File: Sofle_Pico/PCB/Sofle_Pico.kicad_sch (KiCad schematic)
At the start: 81 parts, among them J1 Pimaroni Trackball, J2 4PIN, J3 OLED, J5 Conn_01x05_Socket, J6 Conn_01x05_Socket, Q1 TIP120, SW1 SW_PUSH_LED, SW10 SW_PUSH_LED, SW11 SW_PUSH_LED, SW12 SW_PUSH_LED, SW13 SW_PUSH_LED, SW14 SW_PUSH_LED, SW15 SW_PUSH_LED, SW16 SW_PUSH_LED, SW17 SW_PUSH_LED, SW18 SW_PUSH_LED, SW19 SW_PUSH_LED, SW2 SW_PUSH_LED, SW20 SW_PUSH_LED, SW21 SW_PUSH_LED, SW22 SW_PUSH_LED, SW23 SW_PUSH_LED, SW24 SW_PUSH_LED, SW25 Rotary_Encoder_Switch, SW26 SW_PUSH_LED, SW27 SW_PUSH_LED, SW28 SW_PUSH_LED, SW29 SW_PUSH_LED, SW3 SW_PUSH_LED, SW30 SW_PUSH_LED, SW4 SW_PUSH_LED, SW5 SW_PUSH_LED, SW6 SW_PUSH_LED, SW7 SW_PUSH_LED, SW8 SW_PUSH_LED, SW9 SW_PUSH_LED, U1 SN74AHCT1G125, U3 Pico

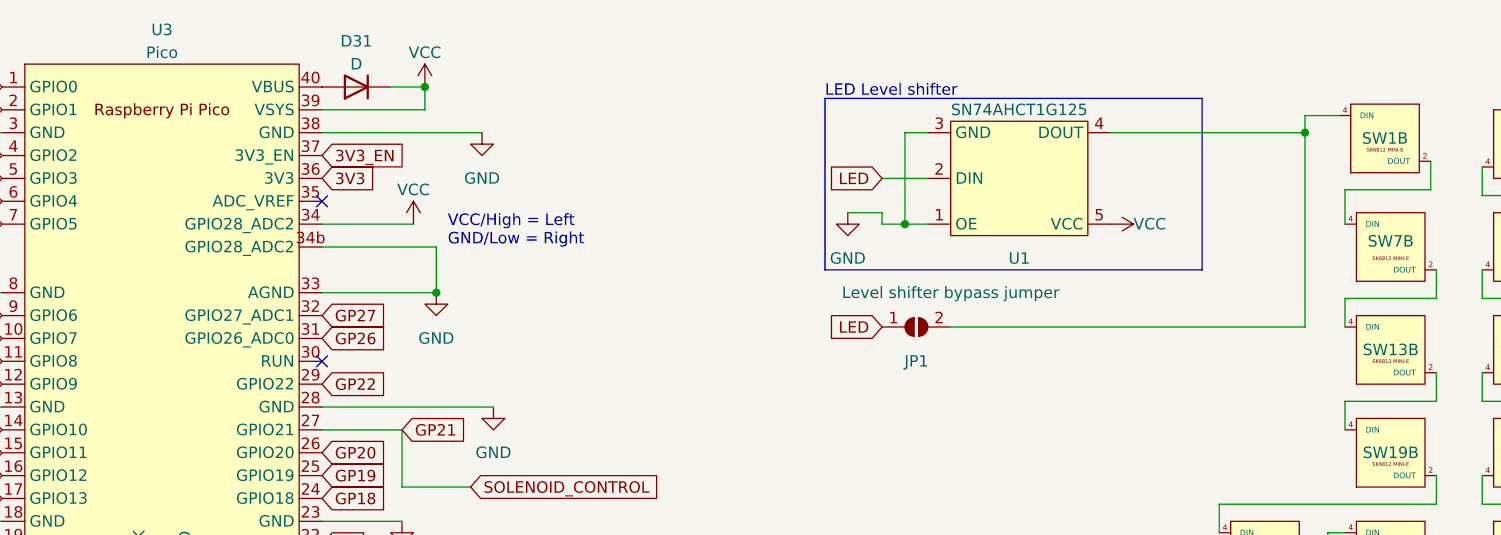
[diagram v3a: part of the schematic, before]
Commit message: Revised LED footprint for better teardrops Tweaked patch bay footprints Tweaked traces for improved zone connections
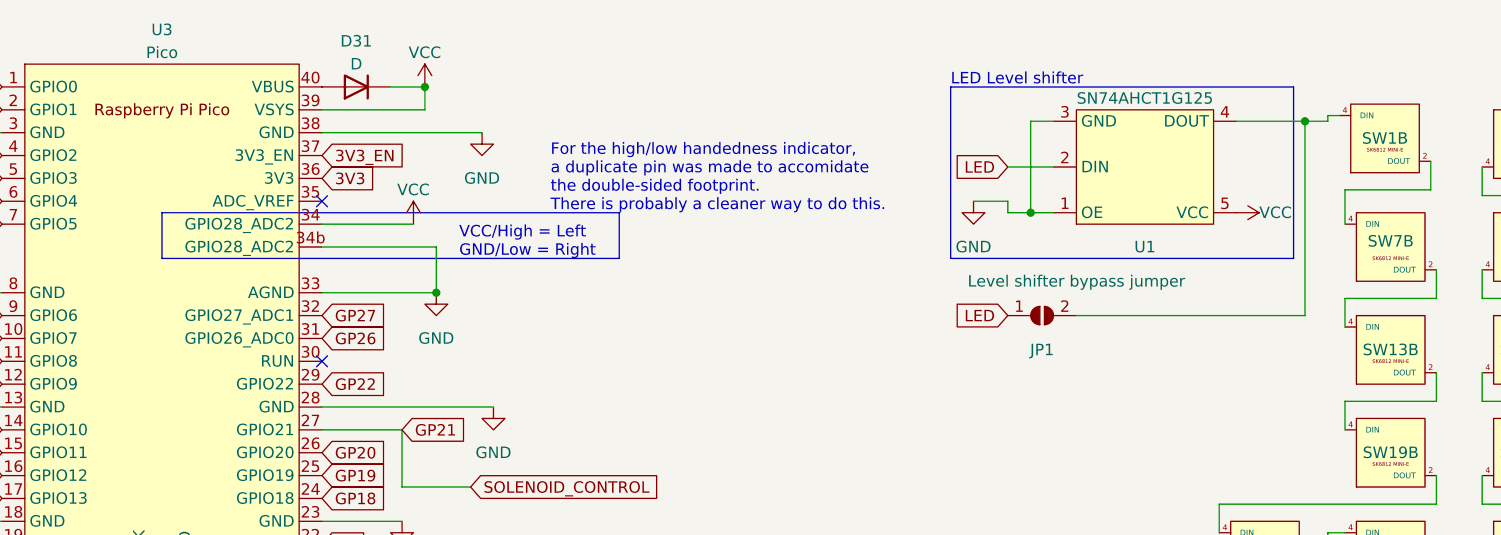
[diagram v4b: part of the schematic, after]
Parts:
- J5: footprint Connector_PinHeader_2.54mm:PinHeader_1x05_P2.54mm_Vertical -> Sofle_Pico:PinHeader_1x05_P2.54mm_Vertical_one-dead
- J6: footprint Connector_PinHeader_2.54mm:PinHeader_1x05_P2.54mm_Vertical -> Sofle_Pico:PinHeader_1x05_P2.54mm_Vertical
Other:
- note added: "For the high/low handedness indicator, a duplicate pin was made to accomidate the double-sided footprint. There is probably a cleaner way to do this."
- moved on the sheet: JP1, U1
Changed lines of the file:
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@@
   (title_block
     (title "Sofle Pico")
-    (date "2023-09-08")
-    (rev "v3.5.1")
+    (date "2023-12-15")
+    (rev "v3.5.2")
     (comment 1 "https://github.com/josefadamcik/SofleKeyboard")
     (comment 2 "Based on the Sofle by Josef Adamcik")
@@
   (junction (at 240.03 114.3) (diameter 0) (color 0 0 0 0)
   )
-  (junction (at 127 36.83) (diameter 0) (color 0 0 0 0)
+  (junction (at 140.97 35.56) (diameter 0) (color 0 0 0 0)
   )
   (junction (at 143.51 139.7) (diameter 0) (color 0 0 0 0)
@@
   (junction (at 199.39 114.3) (diameter 0) (color 0 0 0 0)
   )
+  (junction (at 171.45 25.4) (diameter 0) (color 0 0 0 0)
+  )
   (junction (at 184.15 123.19) (diameter 0) (color 0 0 0 0)
   )
@@
   (junction (at 158.75 147.32) (diameter 0) (color 0 0 0 0)
   )
-  (junction (at 171.45 26.67) (diameter 0) (color 0 0 0 0)
-  )
   (junction (at 163.83 106.68) (diameter 0) (color 0 0 0 0)
   )
@@
     (stroke (width 0) (type default))
   )
+  (wire (pts (xy 171.45 25.4) (xy 173.99 25.4))
+    (stroke (width 0) (type default))
+  )
   (wire (pts (xy 184.15 139.7) (xy 184.15 156.21))
     (stroke (width 0) (type default))
@@
     (stroke (width 0) (type default))
   )
-  (wire (pts (xy 124.46 36.83) (xy 127 36.83))
+  (wire (pts (xy 138.43 35.56) (xy 140.97 35.56))
     (stroke (width 0) (type default))
   )
@@
     (stroke (width 0) (type default))
   )
-  (wire (pts (xy 149.86 26.67) (xy 171.45 26.67))
+  (wire (pts (xy 163.83 25.4) (xy 171.45 25.4))
     (stroke (width 0) (type default))
   )
@@
     (stroke (width 0) (type default))
   )
-  (wire (pts (xy 127 26.67) (xy 129.54 26.67))
+  (wire (pts (xy 140.97 25.4) (xy 143.51 25.4))
     (stroke (width 0) (type default))
   )
@@
     (stroke (width 0) (type default))
   )
-  (wire (pts (xy 171.45 24.765) (xy 175.26 24.765))
+  (wire (pts (xy 173.99 24.765) (xy 175.26 24.765))
     (stroke (width 0) (type default))
   )
@@
     (stroke (width 0) (type default))
   )
-  (wire (pts (xy 129.54 31.75) (xy 124.46 31.75))
+  (wire (pts (xy 143.51 30.48) (xy 138.43 30.48))
     (stroke (width 0) (type default))
   )
@@
     (stroke (width 0) (type default))
   )
-  (wire (pts (xy 171.45 26.67) (xy 171.45 24.765))
+  (wire (pts (xy 173.99 25.4) (xy 173.99 24.765))
     (stroke (width 0) (type default))
   )
@@
     (stroke (width 0) (type default))
   )
-  (wire (pts (xy 132.08 48.26) (xy 171.45 48.26))
+  (wire (pts (xy 146.05 46.99) (xy 171.45 46.99))
     (stroke (width 0) (type default))
   )
@@
     (stroke (width 0) (type default))
   )
-  (wire (pts (xy 120.65 35.56) (xy 124.46 35.56))
+  (wire (pts (xy 134.62 34.29) (xy 138.43 34.29))
     (stroke (width 0) (type default))
   )
@@
     (stroke (width 0) (type default))
   )
-  (wire (pts (xy 124.46 35.56) (xy 124.46 36.83))
+  (wire (pts (xy 138.43 34.29) (xy 138.43 35.56))
     (stroke (width 0) (type default))
   )
@@
     (stroke (width 0) (type default))
   )
-  (wire (pts (xy 171.45 26.67) (xy 171.45 48.26))
+  (wire (pts (xy 171.45 25.4) (xy 171.45 46.99))
     (stroke (width 0) (type default))
   )
@@
     (stroke (width 0) (type default))
   )
-  (wire (pts (xy 127 36.83) (xy 127 26.67))
+  (wire (pts (xy 140.97 35.56) (xy 140.97 25.4))
     (stroke (width 0) (type default))
   )
@@
     (stroke (width 0) (type default))
   )
-  (wire (pts (xy 127 36.83) (xy 129.54 36.83))
+  (wire (pts (xy 140.97 35.56) (xy 143.51 35.56))
     (stroke (width 0) (type default))
   )
@@
     (fill (type none))
   )
-  (rectangle (start 118.11 22.86) (end 160.02 41.91)
+  (rectangle (start 132.08 21.59) (end 170.18 40.64)
     (stroke (width 0) (type default))
     (fill (type none))
@@
     (fill (type none))
   )
+  (rectangle (start 44.45 35.56) (end 95.25 40.64)
+    (stroke (width 0) (type default))
+    (fill (type none))
+  )
   (rectangle (start 13.97 132.08) (end 54.61 156.21)
     (stroke (width 0) (type default))
@@
     (effects (font (size 1.27 1.27)) (justify left bottom))
   )
-  (text "LED Level shifter" (at 118.11 22.86 0)
+  (text "For the high/low handedness indicator, \na duplicate pin was made to accomidate \nthe double-sided footprint. \nThere is probably a cleaner way to do this."
+    (at 87.63 35.56 0)
+    (effects (font (size 1.27 1.27)) (justify left bottom))
+  )
+  (text "LED Level shifter" (at 132.08 21.59 0)
     (effects (font (size 1.27 1.27)) (justify left bottom))
   )
@@
     (effects (font (size 1.27 1.27)) (justify left bottom))
   )
-  (text "VCC/High = Left\nGND/Low = Right" (at 76.2 39.37 0)
+  (text "VCC/High = Left\nGND/Low = Right" (at 77.47 40.64 0)
     (effects (font (size 1.27 1.27)) (justify left bottom))
   )
@@
     )
   )
-  (global_label "LED" (shape input) (at 124.46 31.75 180) (fields_autoplaced)
+  (global_label "LED" (shape input) (at 138.43 30.48 180) (fields_autoplaced)
     (effects (font (size 1.27 1.27)) (justify right))
-    (property "Intersheetrefs" "${INTERSHEET_REFS}" (at 118.1071 31.75 0)
+    (property "Intersheetrefs" "${INTERSHEET_REFS}" (at 132.0771 30.48 0)
       (effects (font (size 1.27 1.27)) (justify right) hide)
     )
@@
     )
   )
-  (global_label "LED" (shape input) (at 124.46 48.26 180) (fields_autoplaced)
+  (global_label "LED" (shape input) (at 138.43 46.99 180) (fields_autoplaced)
     (effects (font (size 1.27 1.27)) (justify right))
-    (property "Intersheetrefs" "${INTERSHEET_REFS}" (at 118.1071 48.26 0)
+    (property "Intersheetrefs" "${INTERSHEET_REFS}" (at 132.0771 46.99 0)
       (effects (font (size 1.27 1.27)) (justify right) hide)
     )
@@
     )
   )
-  (symbol (lib_id "power:VCC") (at 149.86 36.83 270) (unit 1)
+  (symbol (lib_id "power:VCC") (at 163.83 35.56 270) (unit 1)
     (in_bom yes) (on_board yes) (dnp no)
-    (property "Reference" "#PWR016" (at 146.05 36.83 0)
+    (property "Reference" "#PWR016" (at 160.02 35.56 0)
       (effects (font (size 1.27 1.27)) hide)
     )
-    (property "Value" "VCC" (at 152.4 36.83 90)
+    (property "Value" "VCC" (at 166.37 35.56 90)
       (effects (font (size 1.27 1.27)) (justify left))
     )
-    (property "Footprint" "" (at 149.86 36.83 0)
+    (property "Footprint" "" (at 163.83 35.56 0)
       (effects (font (size 1.27 1.27)) hide)
     )
-    (property "Datasheet" "" (at 149.86 36.83 0)
+    (property "Datasheet" "" (at 163.83 35.56 0)
       (effects (font (size 1.27 1.27)) hide)
     )
@@
     )
   )
-  (symbol (lib_id "Junco:SN74AHCT1G125") (at 139.7 31.75 0) (mirror x) (unit 1)
+  (symbol (lib_id "Junco:SN74AHCT1G125") (at 153.67 30.48 0) (mirror x) (unit 1)
     (in_bom yes) (on_board yes) (dnp no)
-    (property "Reference" "U1" (at 139.7 40.64 0)
+    (property "Reference" "U1" (at 153.67 39.37 0)
       (effects (font (size 1.27 1.27)))
     )
-    (property "Value" "SN74AHCT1G125" (at 139.7 24.13 0)
+    (property "Value" "SN74AHCT1G125" (at 153.67 22.86 0)
       (effects (font (size 1.27 1.27)))
     )
-    (property "Footprint" "Sofle_Pico:SN74AHCT1G125 - Junco" (at 139.7 21.59 0)
+    (property "Footprint" "Sofle_Pico:SN74AHCT1G125 - Junco" (at 153.67 20.32 0)
       (effects (font (size 1.27 1.27)) hide)
     )
-    (property "Datasheet" "https://www.ti.com/general/docs/suppproductinfo.tsp?distId=26&gotoUrl=http%3A%2F%2Fwww.ti.com%2Flit%2Fgpn%2Fsn74ahct1g125" (at 139.7 17.78 0)
+    (property "Datasheet" "https://www.ti.com/general/docs/suppproductinfo.tsp?distId=26&gotoUrl=http%3A%2F%2Fwww.ti.com%2Flit%2Fgpn%2Fsn74ahct1g125" (at 153.67 16.51 0)
       (effects (font (size 1.27 1.27)) hide)
     )
@@
       (effects (font (size 1.27 1.27)))
     )
-    (property "Footprint" "Connector_PinHeader_2.54mm:PinHeader_1x05_P2.54mm_Vertical" (at 36.83 140.97 0)
+    (property "Footprint" "Sofle_Pico:PinHeader_1x05_P2.54mm_Vertical" (at 36.83 140.97 0)
       (effects (font (size 1.27 1.27)) hide)
     )
@@
       (effects (font (size 1.27 1.27)))
     )
-    (property "Footprint" "Connector_PinHeader_2.54mm:PinHeader_1x05_P2.54mm_Vertical" (at 16.51 140.97 0)
+    (property "Footprint" "Sofle_Pico:PinHeader_1x05_P2.54mm_Vertical_one-dead" (at 16.51 140.97 0)
       (effects (font (size 1.27 1.27)) hide)
     )
@@
     )
   )
-  (symbol (lib_id "Jumper:SolderJumper_2_Open") (at 128.27 48.26 0) (mirror x) (unit 1)
+  (symbol (lib_id "Jumper:SolderJumper_2_Open") (at 142.24 46.99 0) (mirror x) (unit 1)
     (in_bom yes) (on_board yes) (dnp no)
-    (property "Reference" "JP1" (at 128.27 52.07 0)
+    (property "Reference" "JP1" (at 142.24 50.8 0)
       (effects (font (size 1.27 1.27)))
     )
-    (property "Value" "Level shifter bypass jumper" (at 132.08 44.45 0)
+    (property "Value" "Level shifter bypass jumper" (at 146.05 43.18 0)
       (effects (font (size 1.27 1.27)))
     )
-    (property "Footprint" "Sofle_Pico:Level Shifter Bypass Jumper" (at 128.27 48.26 0)
+    (property "Footprint" "Sofle_Pico:Level Shifter Bypass Jumper" (at 142.24 46.99 0)
       (effects (font (size 1.27 1.27)) hide)
     )
-    (property "Datasheet" "~" (at 128.27 48.26 0)
+    (property "Datasheet" "~" (at 142.24 46.99 0)
       (effects (font (size 1.27 1.27)) hide)
     )
@@
     )
   )
-  (symbol (lib_id "power:GND") (at 120.65 35.56 0) (unit 1)
+  (symbol (lib_id "power:GND") (at 134.62 34.29 0) (unit 1)
     (in_bom yes) (on_board yes) (dnp no) (fields_autoplaced)
-    (property "Reference" "#PWR015" (at 120.65 41.91 0)
+    (property "Reference" "#PWR015" (at 134.62 40.64 0)
       (effects (font (size 1.27 1.27)) hide)
     )
-    (property "Value" "GND" (at 120.65 40.64 0)
+    (property "Value" "GND" (at 134.62 39.37 0)
       (effects (font (size 1.27 1.27)))
     )
-    (property "Footprint" "" (at 120.65 35.56 0)
+    (property "Footprint" "" (at 134.62 34.29 0)
       (effects (font (size 1.27 1.27)) hide)
     )
-    (property "Datasheet" "" (at 120.65 35.56 0)
+    (property "Datasheet" "" (at 134.62 34.29 0)
       (effects (font (size 1.27 1.27)) hide)
     )

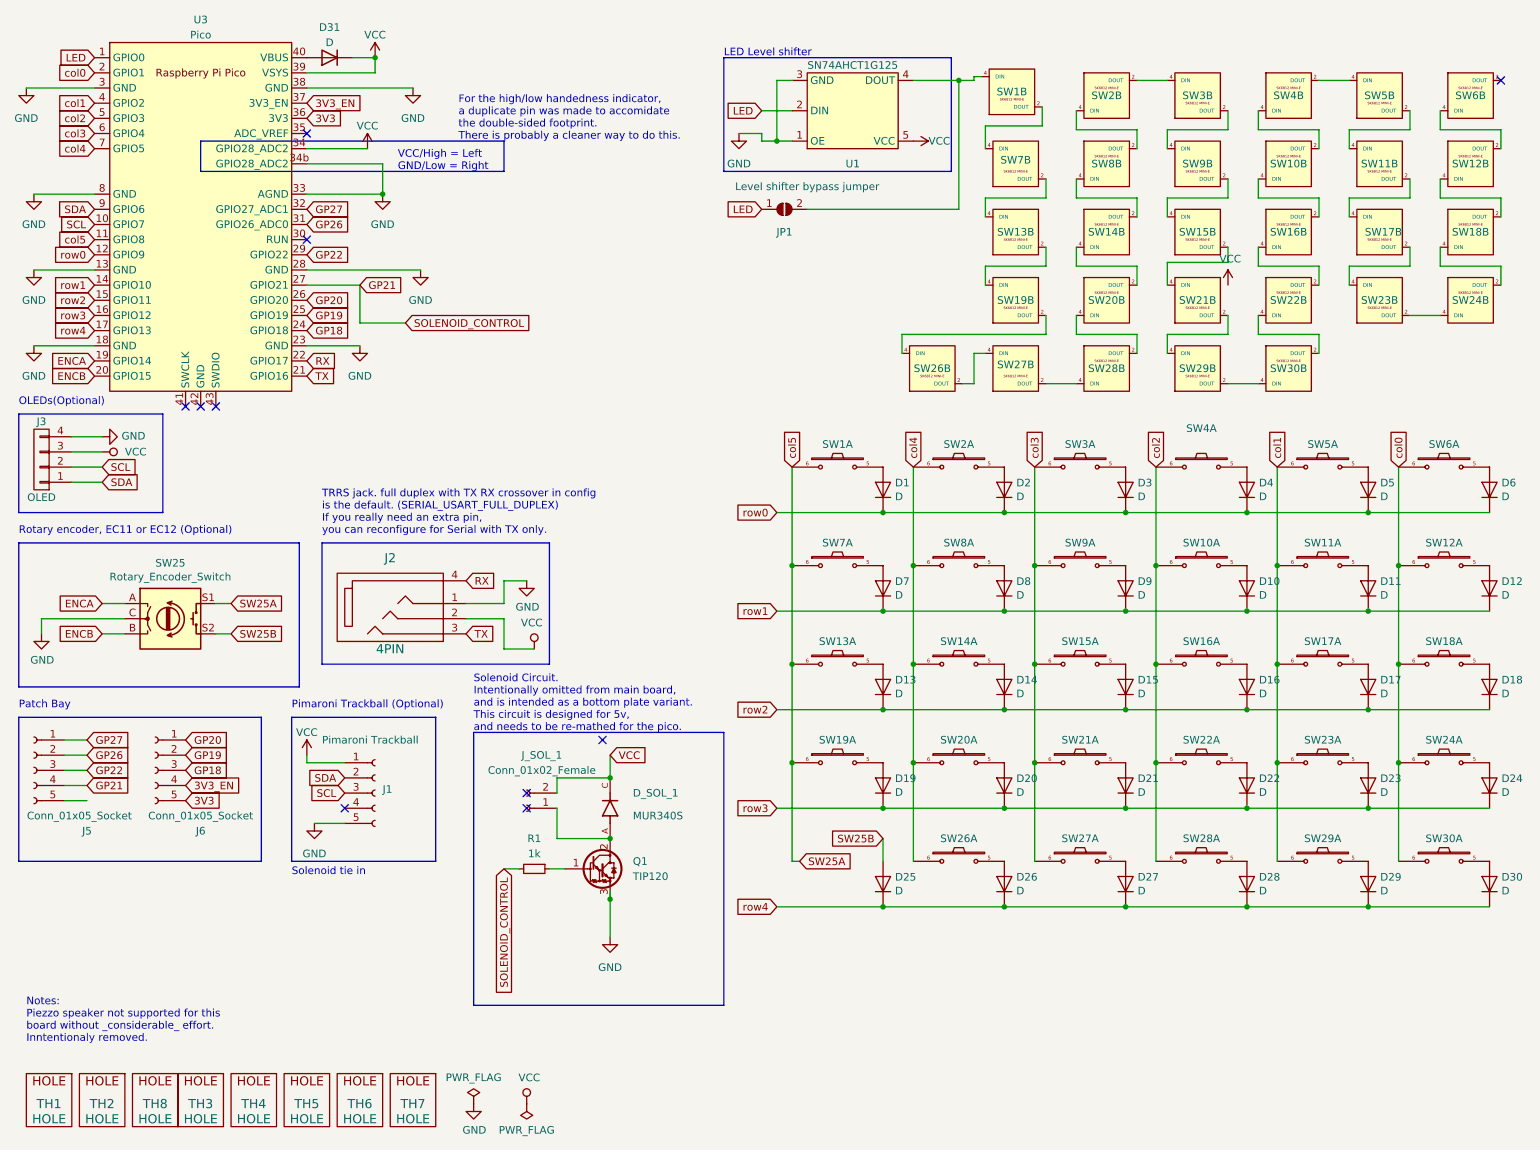
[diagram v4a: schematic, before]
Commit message: Footprint library cleanup
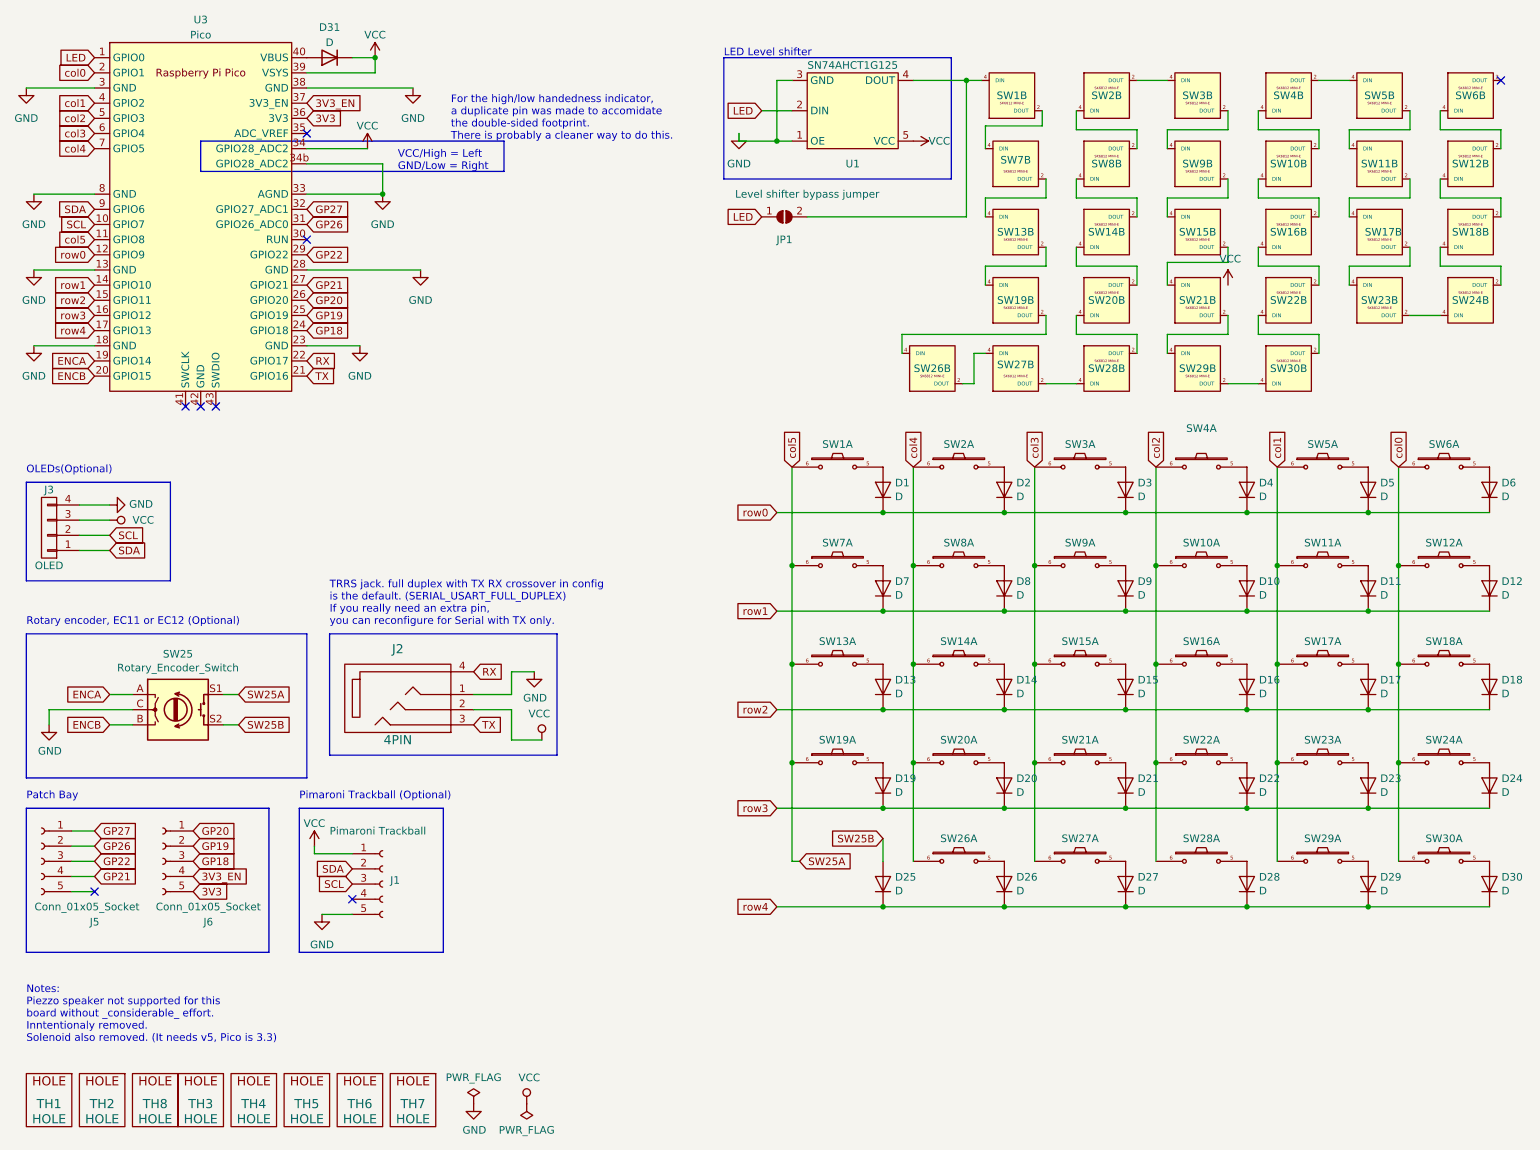
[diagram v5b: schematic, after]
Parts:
- removed D_SOL_1: MUR340S, sofle_v3b:MUR340S_IN4001_TH_HYBRID, symbol MUR340S:MUR340S
- removed J_SOL_1: Conn_01x02_Female, sofle_v3b:PinHeader_1x02_P2.54mm_Vertical, symbol Connector:Conn_01x02_Female
- removed Q1: TIP120, sofle_v3b:TO-220-3_Horizontal_TabUp, symbol Transistor_BJT:TIP120
- removed R1: 1k, Resistor_THT:R_Axial_DIN0309_L9.0mm_D3.2mm_P12.70mm_Horizontal, symbol Device:R_Small
- J3: footprint Sofle_Pico:OLED SSD1306 128x64 UNVERIFIED v3b -> Sofle_Pico:OLED SSD1306 128x64
- U3: footprint Sofle_Pico:RPi_Pico_SMD_TH - Junco -DS Sofle Pico handpins -> Sofle_Pico:RPi_Pico_SMD_TH-DS Sofle Pico handpins
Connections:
- no-connect marks 10 -> 8
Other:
- note added: "Notes: Piezzo speaker not supported for this board without _considerable_ effort. Inntentionaly removed. Solenoid also removed. (It needs v5, Pico is 3.3)"
- note removed: "Notes: Piezzo speaker not supported for this board without _considerable_ effort. Inntentionaly removed."
- note removed: "Solenoid Circuit. Intentionally omitted from main board, and is intended as a bottom plate variant. This circuit is designed for 5v, and needs to be re-mathed for the pico."
- note removed: "Solenoid tie in"
- moved on the sheet: J1, J2, J3, J5, J6, JP1, SW1B, SW25
